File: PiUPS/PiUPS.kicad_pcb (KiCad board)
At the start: 2 copper layers, 87.4 x 56 mm, 112 parts, among them J1 USB_C_Receptacle_USB2.0, J2 USB_B_Micro, J3 Screw_Terminal_01x02, J4 Raspberry_Pi_2_3, J5 USB_A, J6 Screw_Terminal_01x02, Q1 IRF7404, Q2 IRF7404, Q3 IRLML2803TRPBF, Q4 IRF7404, Q5 IRF7404, Q6 IRLML2803TRPBF, Q7 IRLML2803TRPBF, Q8 IRF7404, Q9 IRLML2803TRPBF, SW1 SW_MEC_5E, SW2 MODE (JS102011SAQN), U1 LM393, U2 BQ25895RTW, U3 DW01, U4 FS8205A, U5 TPS61088RHLR, U6 DS3231M

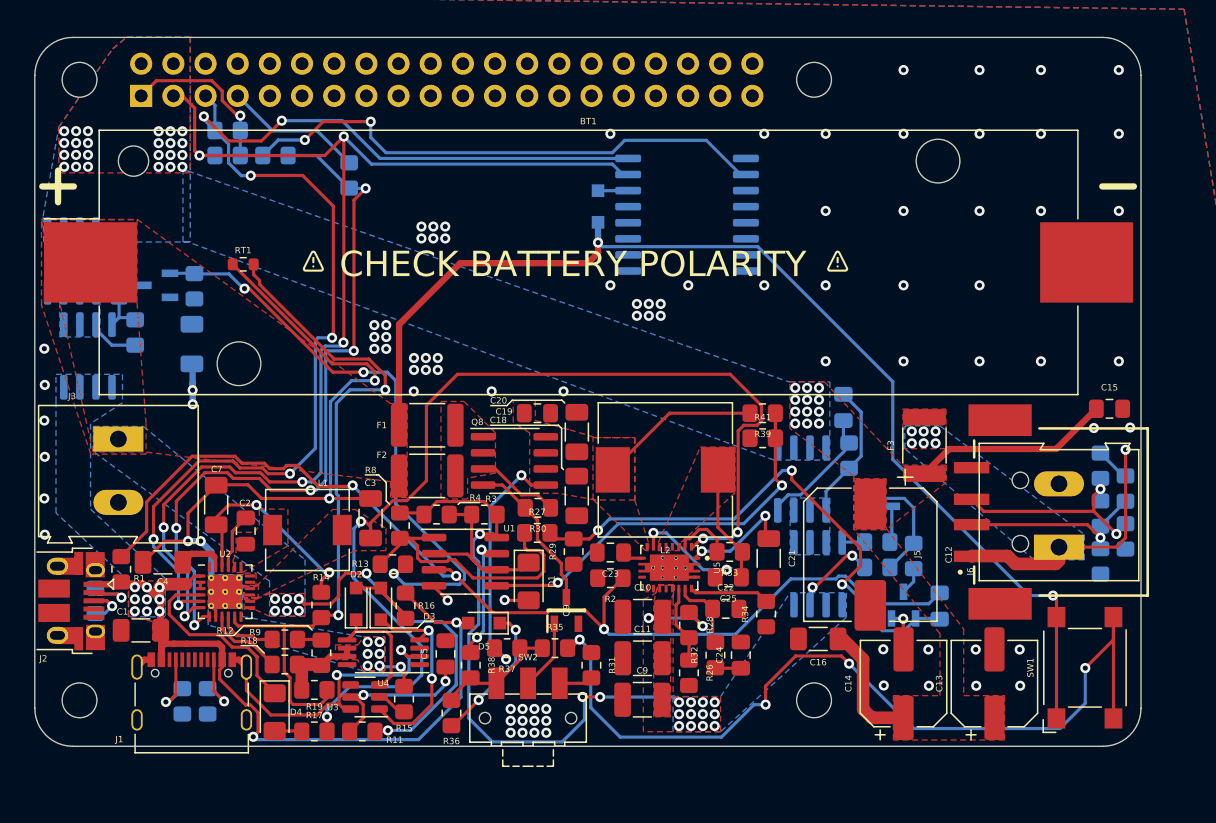
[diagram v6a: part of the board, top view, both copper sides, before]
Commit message: finished routing new PCB
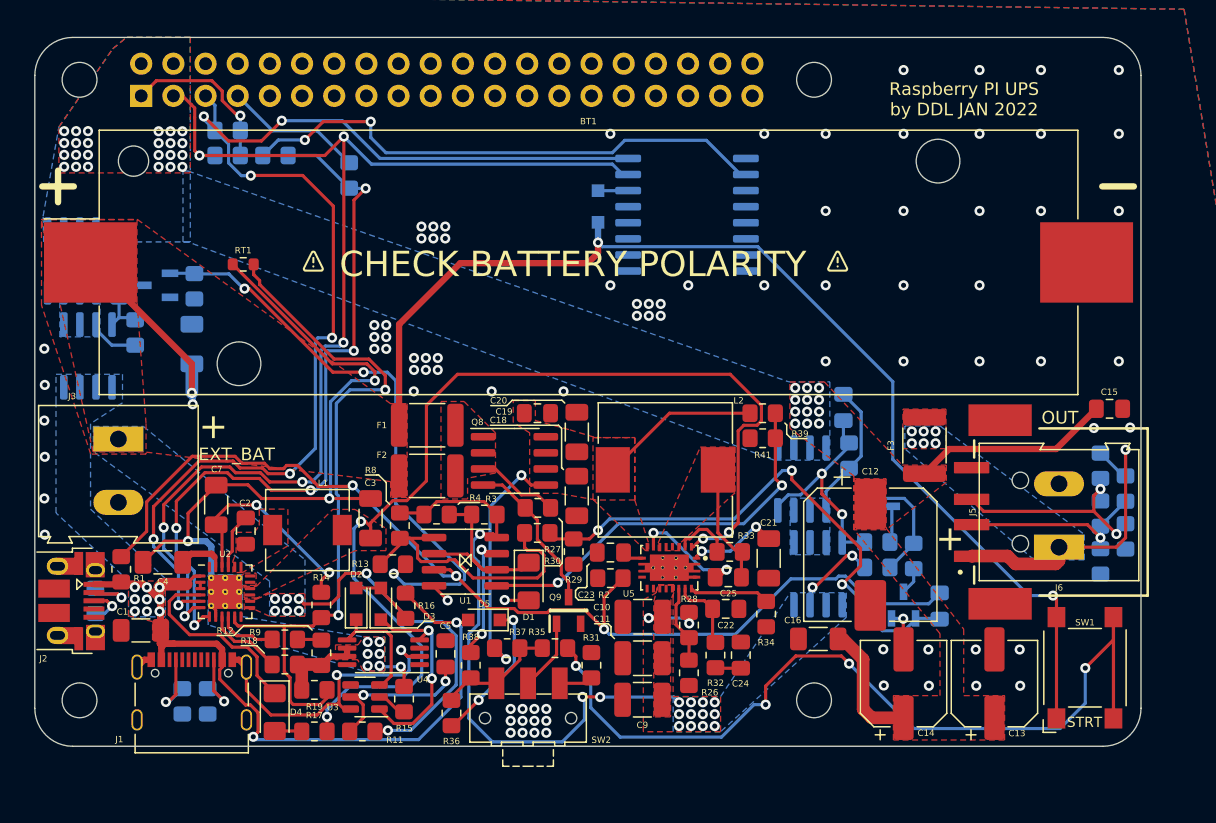
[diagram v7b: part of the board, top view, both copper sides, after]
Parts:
- moved D5 0.25 mm to (101.9, 113.4)
- moved Q9 0.17 mm to (108.5, 112.7)
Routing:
- net +BATT: track 121.4 -> 134.5 mm
- net Net-(C8-Pad2): track 12.0 -> 18.1 mm, vias 0 -> 2
- net VOUT: track 61.6 -> 59.8 mm
- net Net-(C21-Pad1): track 8.91 -> 7.18 mm
- net Net-(R35-Pad2): track 69.4 -> 67.9 mm
- net GND1: track 64.7 -> 64.5 mm, vias 11 -> 10
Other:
- board text added: "+"
- board text added: "EXT_BAT"
- board text added: "OFF"
- board text added: "ON"
- board text added: "OUT"
- board text added: "Place this diode to enable RTC"
- board text added: "Place this shunt to enable INT signal"
- board text added: "Raspberry PI UPS by DDL JAN 2022"
- board text added: "STRT"

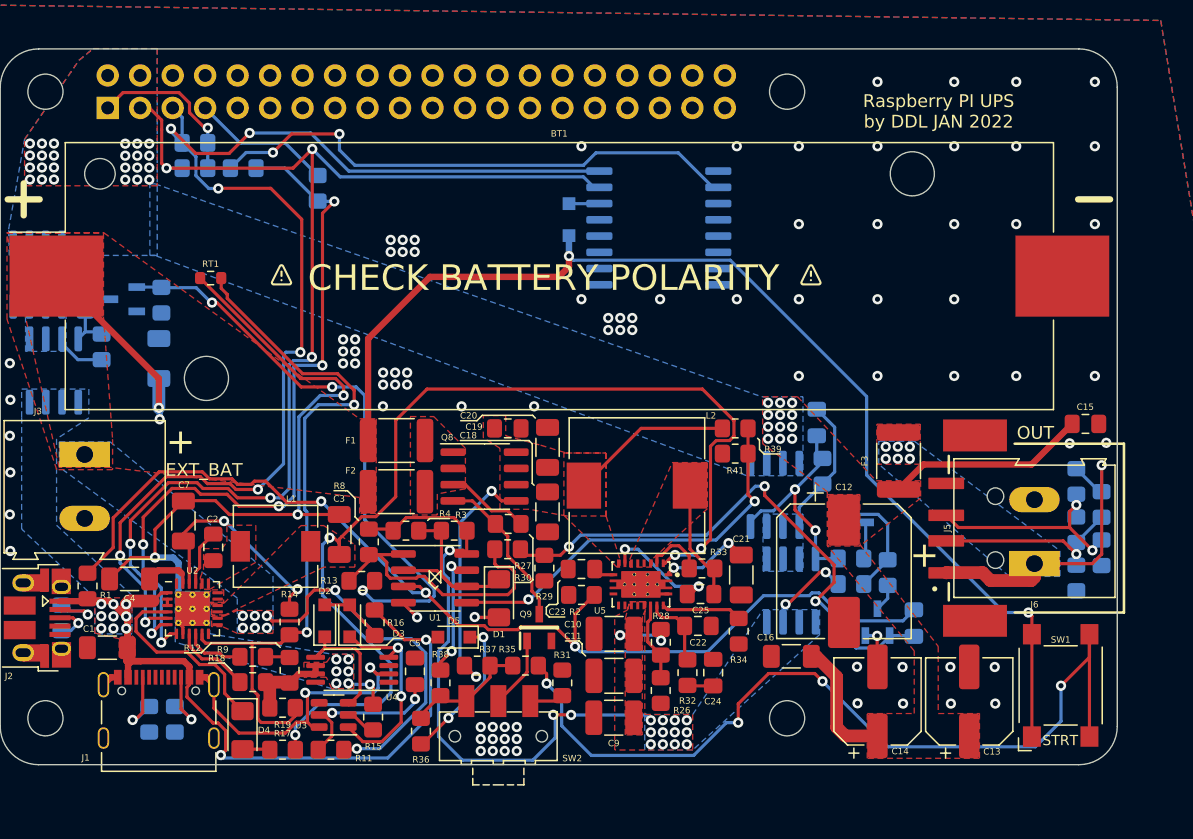
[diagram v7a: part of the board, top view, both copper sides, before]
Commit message: Fixed DRC issues
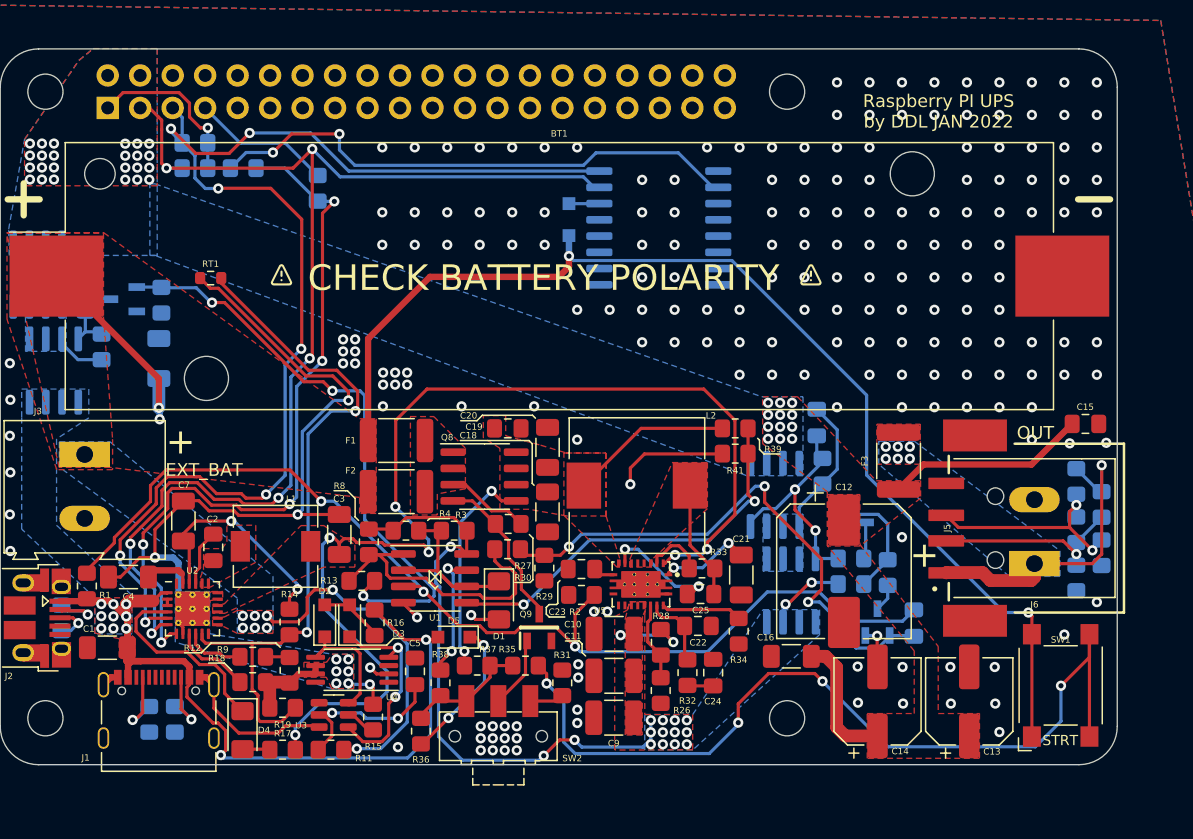
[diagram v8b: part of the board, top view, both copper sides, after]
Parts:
- moved C4 0.17 mm to (76.4, 108.7)
- moved D1 0.16 mm to (105.4, 110.5)
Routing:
- net VSYS: track 83.3 -> 89.6 mm, vias 4 -> 6
- net Net-(C18-Pad1): track 32.3 -> 29.8 mm
- net +BATT: track 134.5 -> 132.9 mm
- net Net-(R14-Pad1): track 56.0 -> 54.9 mm
- net GND: track 34.4 -> 33.4 mm, vias 87 -> 197
- net +5V: track 61.6 -> 62.6 mm
- net INT: track 58.3 -> 57.4 mm
- net VOUT: track 59.8 -> 60.6 mm
- net Net-(R35-Pad2): track 67.9 -> 68.5 mm
- net SCL: track 99.8 -> 100.4 mm
